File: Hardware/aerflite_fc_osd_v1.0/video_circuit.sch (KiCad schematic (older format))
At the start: 28 parts, among them Q1 MMUN2211LT1-D, U3 MCP6562, U4 FMS6141, U5 SN74LVC1G04, U6 74LVC1G3157

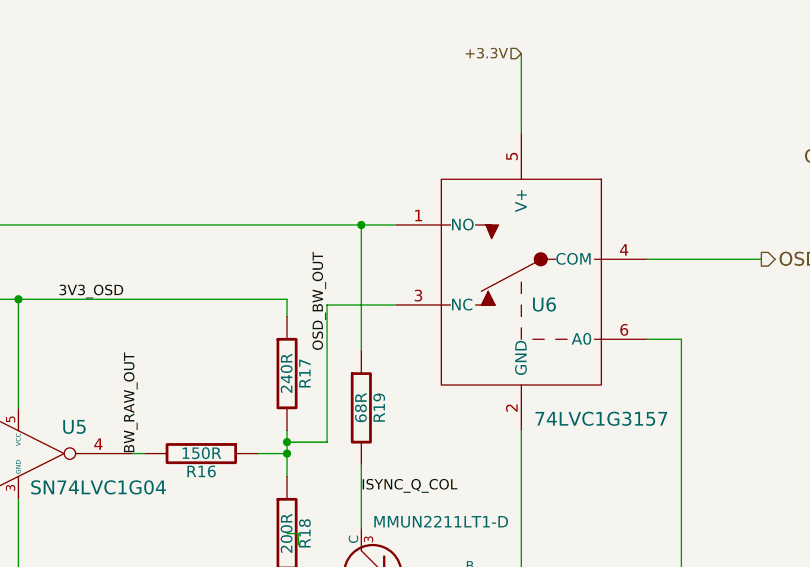
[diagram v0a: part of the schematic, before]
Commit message: rewrite schematic, did ERC and DRC, but no real changes
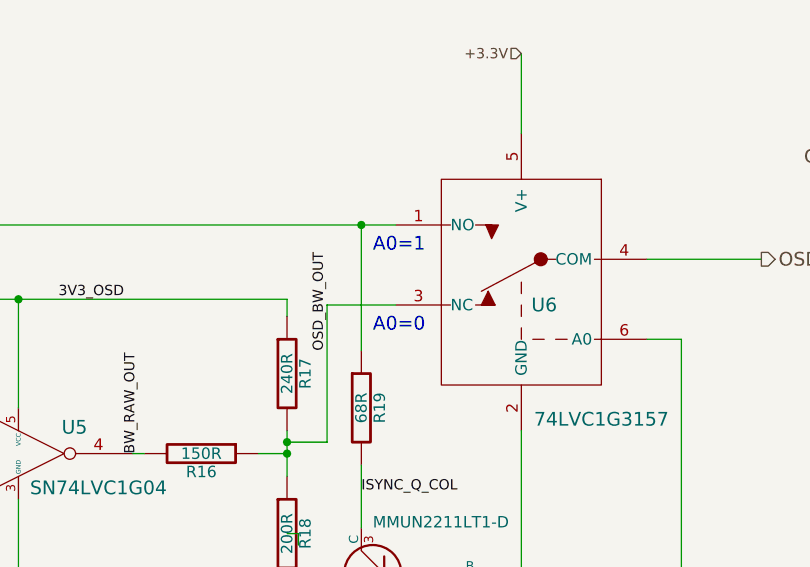
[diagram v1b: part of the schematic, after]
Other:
- note added: "A0=0"
- note added: "A0=1"
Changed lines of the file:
@@
 LIBS:siliconi
 LIBS:contrib
-LIBS:si80655
-LIBS:fms6141
-LIBS:tja1051t
-LIBS:conn_5
-LIBS:si8065
 LIBS:osd-cache
 EELAYER 25 0
@@
 	6250 2800 6250 2325
 Connection ~ 6250 2325
+Text Notes 8250 2125 0    60   ~ 0
+A0=1
+Text Notes 8250 2475 0    60   ~ 0
+A0=0
 $EndSCHEMATC

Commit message: update kicad fc_osd_v1 for later kicad version
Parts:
- U3: symbol MCP6562 -> MCP6562-RESCUE-osd
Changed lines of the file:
@@
 EESchema Schematic File Version 2
+LIBS:osd-rescue
 LIBS:power
 LIBS:device
@@
 Csync circuit
 $Comp
-L MCP6562 U3
+L MCP6562-RESCUE-osd U3
 U 3 1 54707205
 P 10700 1200
+AR Path="/54707205" Ref="U3"  Part="3"
+AR Path="/573F746B/573F7492/54707205" Ref="U3"  Part="3"
 F 0 "U3" H 10750 1400 60  0000 L CNN
 F 1 "MCP6562" H 10650 1000 60  0000 L CNN
@@
 $EndComp
 $Comp
-L MCP6562 U3
+L MCP6562-RESCUE-osd U3
 U 2 1 54706BB6
 P 5200 6400
+AR Path="/54706BB6" Ref="U3"  Part="2"
+AR Path="/573F746B/573F7492/54706BB6" Ref="U3"  Part="2"
 F 0 "U3" H 5250 6600 60  0000 L CNN
 F 1 "MCP6562" H 5150 6200 60  0000 L CNN
@@
 $EndComp
 $Comp
-L MCP6562 U3
+L MCP6562-RESCUE-osd U3
 U 1 1 54706B91
 P 2450 6200
+AR Path="/54706B91" Ref="U3"  Part="1"
+AR Path="/573F746B/573F7492/54706B91" Ref="U3"  Part="1"
 F 0 "U3" H 2500 6400 60  0000 L CNN
 F 1 "MCP6562" H 2400 6000 60  0000 L CNN
